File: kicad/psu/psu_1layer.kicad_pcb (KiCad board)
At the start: 2 copper layers, 117 x 65 mm, 35 parts, among them J1 AC IN 12-15V, J2 DC IN 12V, J3 DC OUT 1, J4 DC OUT 2, J5 LED REMOTE, Q1 BC547, Q2 TIP41C, Q3 BC547

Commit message: Rotate screw terminals to face the board edge, add 3D views, schematics and layouts to the README, CircuitJS links in the review
Amp board is 100 x 85 mm after the hybrid-footprint courtyards grew; input header moved to open space
on the bottom edge so freerouting completes. Panel 134 x 137 mm, DRC clean.
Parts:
- removed JL1: wire link, Custom:WireLink
- moved J2 6.50 mm to (158.6, 66.9), turned to 90 degrees
- moved J3 6.50 mm to (158.6, 85.1), turned to 90 degrees
- moved J4 6.50 mm to (158.6, 103.3), turned to 90 degrees
- moved C1 2.60 mm to (118.0, 69.2)
- moved C2 2.60 mm to (136.7, 69.2)
- moved D1 1.30 mm to (68.4, 66.8)
- moved D2 1.30 mm to (91.5, 66.8)
- moved D3 1.30 mm to (68.4, 75.4)
- moved D4 1.30 mm to (91.5, 75.4)
- moved J1 0.65 mm to (57.8, 68.2), turned to -90 degrees
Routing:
- net GND: track 333.3 -> 287.7 mm
- net Net-(D6-A): track 198.1 -> 158.6 mm
- net /AC1: track 69.6 -> 35.2 mm
- net Net-(D1-K): track 255.6 -> 287.2 mm
- net /AC2: track 60.5 -> 81.0 mm
- net Net-(Q1-E): track 112.7 -> 99.7 mm
- net Net-(D8-A): track 38.8 -> 29.0 mm
- net /VZ: track 76.6 -> 84.9 mm
- net Net-(J1-Pin_1): track 27.1 -> 21.3 mm
- net Net-(D7-A): track 24.6 -> 30.2 mm
- net Net-(Q2-E): track 158.5 -> 154.2 mm

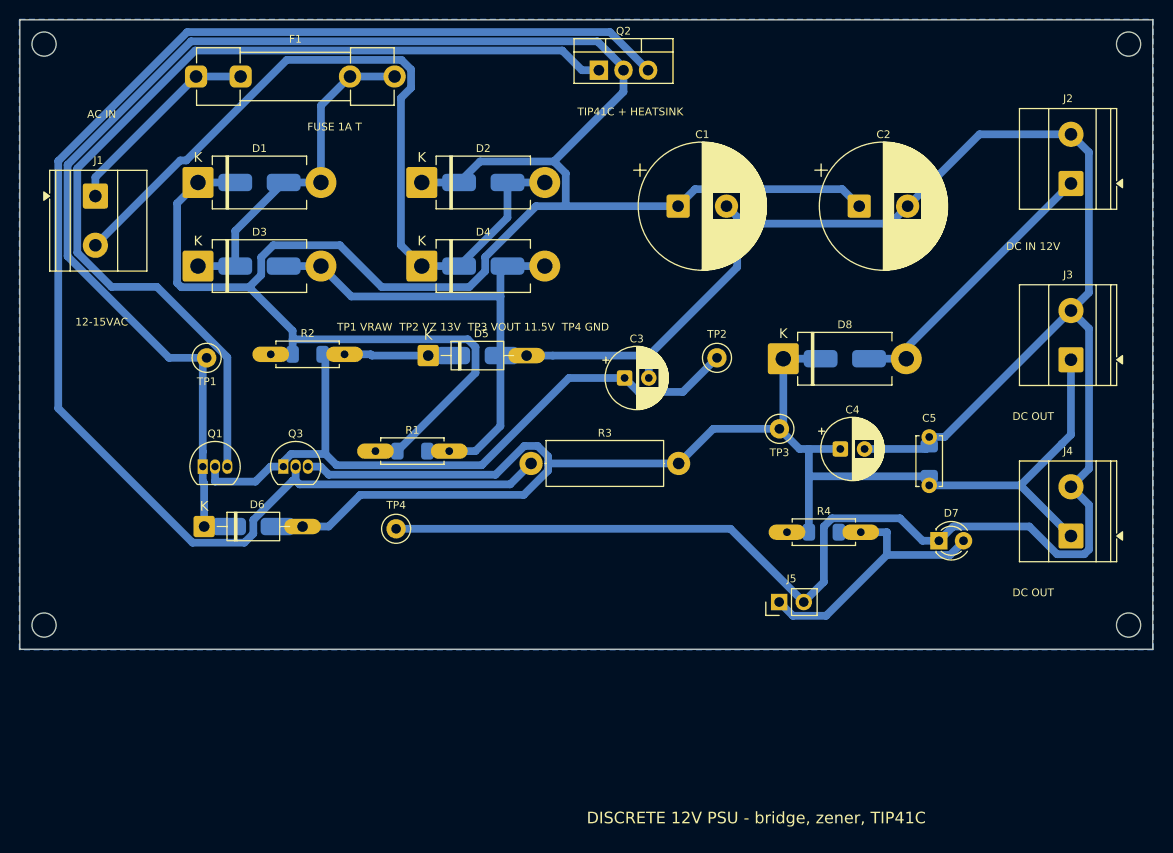
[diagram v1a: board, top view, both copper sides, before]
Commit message: Square 144 x 144 mm panel with rails; amp widened to 134 x 71 mm so PSU plus volume board match its width; readable silkscreen
References sit inside resistor, diode and ceramic outlines along the body axis, larger text; electrolytic,
transistor and test-point labels stay beside the part. Hybrid footprints built from the library parts keep
polarity marks. All 2-layer boards, the panel and the single-sided PSU and volume boards are DRC clean.
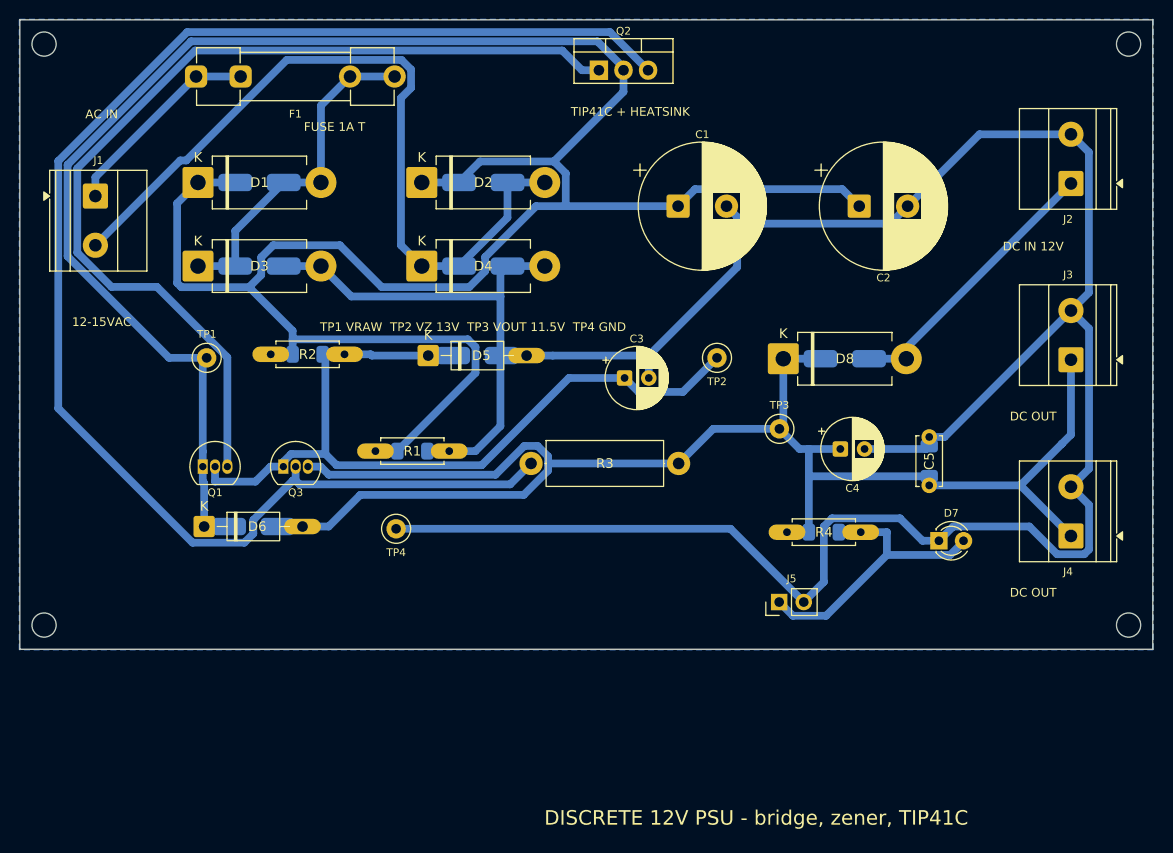
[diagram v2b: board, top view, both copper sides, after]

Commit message: Repository URL and revision on every silkscreen and on the panel rails
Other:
- board text added: "discrete-stereo-amp v1.0 2026-10"
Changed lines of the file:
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@@
+		)
+	)
+	(gr_text "discrete-stereo-amp v1.0 2026-10"
+		(at 131.95 52.45 0)
+		(layer "F.SilkS")
+		(effects
+			(font
+				(size 0.9 0.9)
+				(thickness 0.15)
+			)
 		)
 	)

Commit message: Release 1.1: square panel, rotated terminals, readable silkscreen, URL and revision stamps
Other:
- board text added: "discrete-stereo-amp v1.1 2026-10"
- board text removed: "discrete-stereo-amp v1.0 2026-10"
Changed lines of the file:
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@@
 		)
 	)
-	(gr_text "discrete-stereo-amp v1.0 2026-10"
+	(gr_text "discrete-stereo-amp v1.1 2026-10"
 		(at 131.95 52.45 0)
 		(layer "F.SilkS")

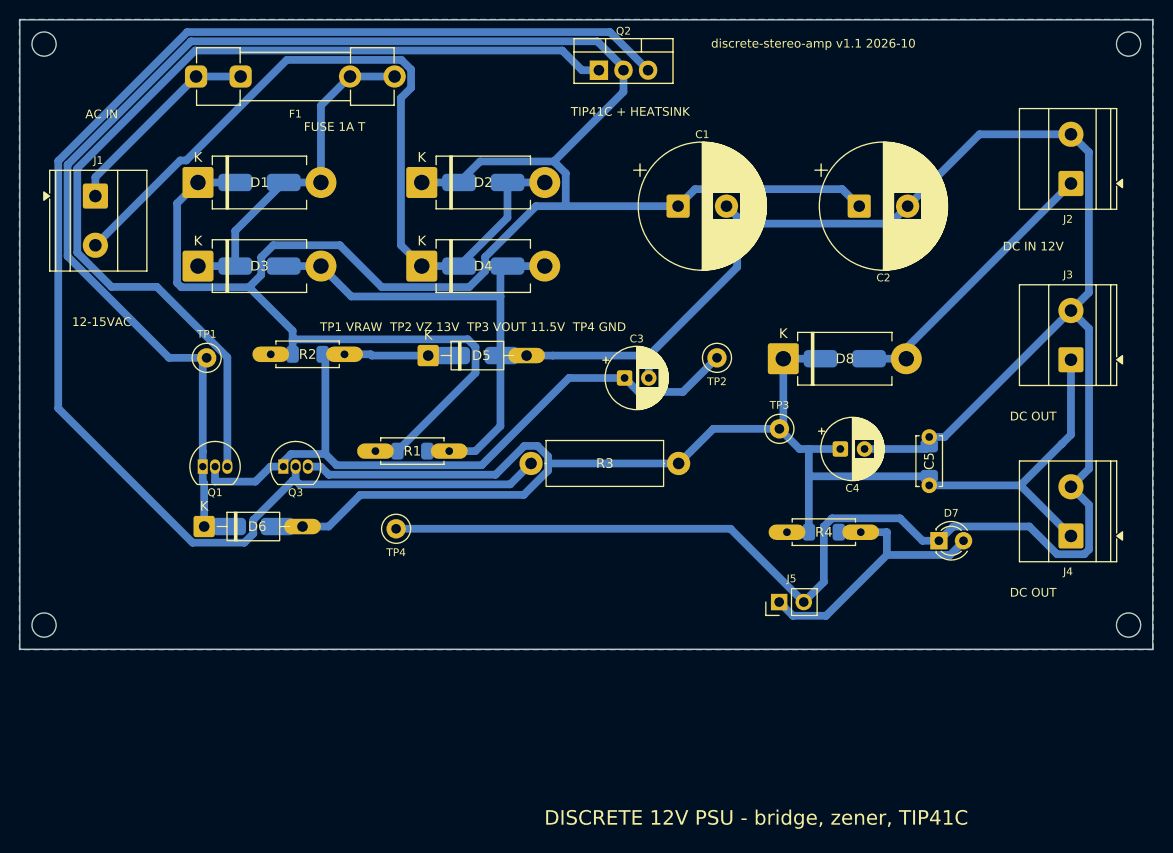
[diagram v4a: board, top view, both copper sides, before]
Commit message: Release 1.2: mirror-loaded front end, closed-loop PSU, VU tap, headphone board
- Amp: PNP input pair with NPN current-mirror load, LED-referenced current-source tail,
  NPN VAS with bootstrapped load from +12V, 220p Miller + 47p lead cap (THD 0.004% at 26 mW/8R,
  0.019% at 0.29 W; was 0.03 / 0.2). 1k VU meter tap per channel to header J5.
- PSU: BC547 error amplifier, 5.6 V zener fed from VOUT, 8.2k + 2k trimmer / 10k divider,
  2.2k drive, 47n/100n compensation. 12.0 V set point, 0.14 V dip on a 1 A step.
- New headphone board (DPDT switch, 120R series, DIRECT jumpers, 3.5 mm jack, panel-jack header).
- Boards: amp 134x85 / compact 100x98, PSU 90x58, hp 42x30; panel 155x155 with four boards.
  All 2-layer boards and the panel DRC clean; single-sided amp down to 15 errors.
- Toolchain: STAMP constant, reroute.sh second routing pass, rotated titles, link holes on
  jumper pads, 2 mm routing corridor per channel.
- Docs, BOMs, order guide, changelog, known issues rewritten for release 2.
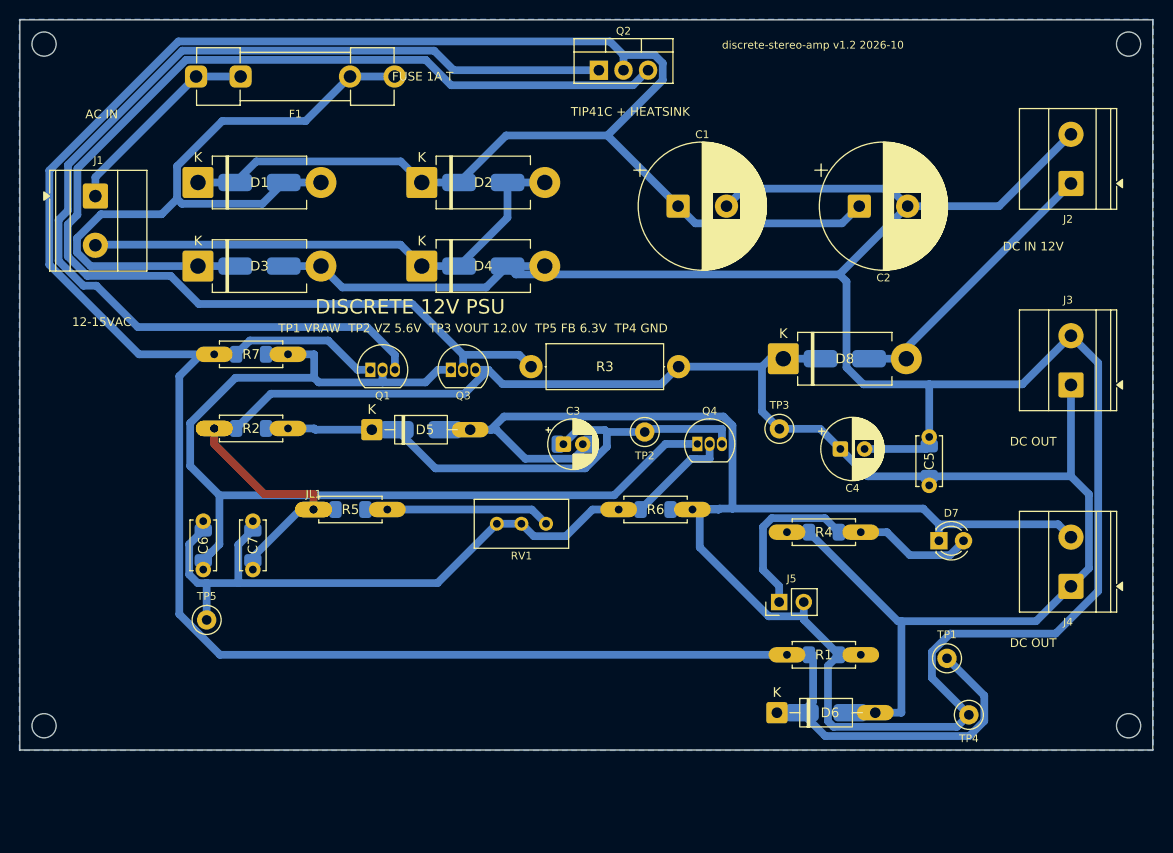
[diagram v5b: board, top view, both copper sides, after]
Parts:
- added C6: 47n, Custom:C_P5_1206, F.Cu at (68.9, 106.8)
- added C7: 100n, Custom:C_P5_1206, F.Cu at (74.1, 106.8)
- added JL1: wire link, Custom:WireLink, F.Cu at (80.3, 100.6)
- added Q4: BC547, Custom:TO92_SOT23, F.Cu at (120.0, 93.8)
- added R5: 8.2k, Custom:R_Axial_1206, F.Cu at (80.3, 100.6)
- added R6: 10k, Custom:R_Axial_1206, F.Cu at (111.8, 100.6)
- added R7: 2.2k, Custom:R_Axial_1206, F.Cu at (70.1, 84.5)
- added RV1: 2k, Potentiometer_THT:Potentiometer_Bourns_3296W_Vertical, F.Cu at (104.3, 102.0)
- added TP5: FB 6.3V, TestPoint:TestPoint_Loop_D2.50mm_Drill1.0mm, F.Cu at (69.3, 112.0)
- C3: value 100u -> 10u; footprint Capacitor_THT:CP_Radial_D6.3mm_P2.50mm -> Custom:CE_P2_1206
- D5: value 13V 1W -> 5.6V
- TP2: value VZ 13V -> VZ 5.6V
- TP3: value VOUT 11.5V -> VOUT 12.0V
- moved TP1 82.5 mm to (145.7, 115.9)
- moved D6 62.2 mm to (128.2, 121.6)
- moved TP4 62.2 mm to (148.0, 121.8)
- moved R1 47.4 mm to (129.2, 115.6)
- moved Q1 20.0 mm to (86.2, 86.1)
- moved Q3 20.0 mm to (94.5, 86.1)
- moved TP2 10.7 mm to (114.5, 92.6)
- moved H3 10.4 mm to (52.5, 122.9)
- moved H4 10.4 mm to (164.5, 122.9)
- moved R3 10.00 mm to (102.8, 85.8)
- moved R2 9.63 mm to (70.1, 92.2)
- moved D5 9.62 mm to (86.3, 92.3)
- moved C3 9.31 mm to (106.1, 93.8)
- moved J4 5.20 mm to (158.6, 108.5)
- moved J3 2.60 mm to (158.6, 87.7)
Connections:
- C3 pad 1: /VZ -> Net-(D5-K)
- D5 pad 1: /VZ -> Net-(D5-K)
- D5 pad 1S: /VZ -> Net-(D5-K)
- Q1 pad 2: /VZ -> /BQ1
- Q3 pad 1: /VZ -> /BQ1
- R2 pad 1: Net-(D1-K) -> Net-(D6-A)
- R2 pad 1S: Net-(D1-K) -> Net-(D6-A)
- R2 pad 2: /VZ -> Net-(D5-K)
- R2 pad 2S: /VZ -> Net-(D5-K)
- TP2 pad 1: /VZ -> Net-(D5-K)
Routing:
- net /BQ1: track 0.00 -> 108.1 mm
- net /VZ: track 84.9 -> 0.00 mm
- net Net-(Q4-B): track 0.00 -> 79.0 mm
- net GND: track 287.7 -> 365.6 mm
- net Net-(D5-K): track 0.00 -> 58.7 mm
- net Net-(D1-K): track 287.2 -> 338.9 mm
- net Net-(D6-A): track 158.6 -> 207.5 mm
- net /AC1: track 35.2 -> 76.1 mm
- net /AC2: track 81.0 -> 53.1 mm
- net Net-(Q2-E): track 154.2 -> 128.9 mm
- net Net-(R5-Pad2): track 0.00 -> 19.3 mm
- net Net-(Q1-E): track 99.7 -> 111.2 mm
- net Net-(D7-A): track 30.2 -> 31.8 mm
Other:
- board size 117 x 65 mm -> 117 x 75.4 mm
- board text added: "DISCRETE 12V PSU"
- board text added: "TP1 VRAW TP2 VZ 5.6V TP3 VOUT 12.0V TP5 FB 6.3V TP4 GND"
- board text added: "discrete-stereo-amp v1.2 2026-10"
- board text removed: "DISCRETE 12V PSU - bridge, zener, TIP41C"
- board text removed: "TP1 VRAW TP2 VZ 13V TP3 VOUT 11.5V TP4 GND"
- board text removed: "discrete-stereo-amp v1.1 2026-10"
